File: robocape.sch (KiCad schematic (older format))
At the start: 14 parts

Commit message: Schematics: PWM
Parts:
- added R? (x2): 4.7k, symbol R_Small
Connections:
- net I2C2_SCL: now also R?.2
- net I2C2_SDA: now also R?.2
- net EHRPWM2B: now reaches U?.B13 (EHRPWM2B)
- net EHRPWM2A: now reaches U?.B19 (EHRPWM2A)
- net EHRPWM0B: now reaches U?.C21 (UART2_TXD)
- net PWMGEN_OE: now reaches U?.C25 (GPIO3_21)
- net EHRPWM1A: now reaches U?.C14 (EHRPWM1A)
- net EHRPWM1B: now reaches U?.C16 (EHRPWM1B)
- net EHRPWM0A: now reaches U?.C22 (UART2_RXD)
- new net +3.3V_A: R?.1, R?.1
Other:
- note added: "0 ohm resistors \nto select address\non i2c bus: 0x54 to 0x57\n"
- note added: "I2C adresses:\nEEPROM: 0x54 to 0x57\nBarometer: 0x77\n"
- note added: "I2C pull-ups\n"
- note removed: "0 ohm resistors \nto select address\non i2c bus"
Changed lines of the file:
@@
 F5 "XBEE_RTS" I R 3925 6250 39
 F6 "XBEE_DTR" I R 3925 6300 39
+F7 "I2C2_SDA" I R 3925 6400 39
+F8 "I2C2_SCL" I R 3925 6450 39
+F9 "PWMGEN_OE" I R 3925 6500 39
+F10 "PWM_0" I R 3925 6600 39
+F11 "PWM_1" I R 3925 6650 39
+F12 "PWM_3" I R 3925 6750 39
+F13 "PWM_4" I R 3925 6800 39
+F14 "PWM_2" I R 3925 6700 39
+F15 "PWM_5" I R 3925 6850 39
 $EndSheet
 $Sheet
@@
 	9775 1200 9775 1225
 Text Notes 10250 1400 0    39   ~ 0
-0 ohm resistors \nto select address\non i2c bus
+0 ohm resistors \nto select address\non i2c bus: 0x54 to 0x57\n
 Wire Wire Line
 	9475 1925 9425 1925
@@
 Wire Wire Line
 	4700 2875 4750 2875
+Text Notes 1200 4700 0    47   ~ 0
+I2C adresses:\nEEPROM:	0x54 to 0x57\nBarometer:	0x77\n
+Text Label 8475 3550 2    39   ~ 0
+I2C2_SDA
+Text Label 8475 3600 2    39   ~ 0
+I2C2_SCL
+$Comp
+L R_Small R?
+U 1 1 55A80D7C
+P 8575 3400
+F 0 "R?" H 8605 3420 50  0000 L CNN
+F 1 "4.7k" H 8605 3360 50  0000 L CNN
+F 2 "" H 8575 3400 60  0000 C CNN
+F 3 "" H 8575 3400 60  0000 C CNN
+	1    8575 3400
+	1    0    0    -1
+$EndComp
+$Comp
+L R_Small R?
+U 1 1 55A80E92
+P 8825 3400
+F 0 "R?" H 8855 3420 50  0000 L CNN
+F 1 "4.7k" H 8855 3360 50  0000 L CNN
+F 2 "" H 8825 3400 60  0000 C CNN
+F 3 "" H 8825 3400 60  0000 C CNN
+	1    8825 3400
+	1    0    0    -1
+$EndComp
+Wire Wire Line
+	8475 3550 8575 3550
+Wire Wire Line
+	8575 3550 8575 3500
+Wire Wire Line
+	8475 3600 8825 3600
+Wire Wire Line
+	8825 3600 8825 3500
+$Comp
+L +3.3V_A #PWR?
+U 1 1 55A80FFB
+P 8575 3250
+F 0 "#PWR?" H 8575 3210 30  0001 C CNN
+F 1 "+3.3V_A" H 8575 3360 30  0000 C CNN
+F 2 "" H 8575 3250 60  0000 C CNN
+F 3 "" H 8575 3250 60  0000 C CNN
+	1    8575 3250
+	1    0    0    -1
+$EndComp
+Wire Wire Line
+	8575 3250 8575 3300
+$Comp
+L +3.3V_A #PWR?
+U 1 1 55A810F5
+P 8825 3250
+F 0 "#PWR?" H 8825 3210 30  0001 C CNN
+F 1 "+3.3V_A" H 8825 3360 30  0000 C CNN
+F 2 "" H 8825 3250 60  0000 C CNN
+F 3 "" H 8825 3250 60  0000 C CNN
+	1    8825 3250
+	1    0    0    -1
+$EndComp
+Wire Wire Line
+	8825 3250 8825 3300
+Text Notes 8200 3050 0    39   ~ 0
+I2C pull-ups\n
+Text Label 6550 2575 0    39   ~ 0
+EHRPWM0A
+Wire Wire Line
+	6550 2575 6500 2575
+Text Label 4700 2575 2    39   ~ 0
+EHRPWM0B
+Wire Wire Line
+	4700 2575 4750 2575
+Text Label 6550 2175 0    39   ~ 0
+EHRPWM1A
+Text Label 6550 2275 0    39   ~ 0
+EHRPWM1B
+Wire Wire Line
+	6550 2275 6500 2275
+Wire Wire Line
+	6500 2175 6550 2175
+Text Label 1750 2475 2    39   ~ 0
+EHRPWM2A
+Wire Wire Line
+	1800 2475 1750 2475
+Text Label 1750 2175 2    39   ~ 0
+EHRPWM2B
+Wire Wire Line
+	1750 2175 1800 2175
+Text Label 3975 6600 0    39   ~ 0
+EHRPWM0A
+Wire Wire Line
+	3975 6600 3925 6600
+Text Label 3975 6650 0    39   ~ 0
+EHRPWM0B
+Text Label 3975 6700 0    39   ~ 0
+EHRPWM1A
+Text Label 3975 6750 0    39   ~ 0
+EHRPWM1B
+Text Label 3975 6800 0    39   ~ 0
+EHRPWM2A
+Text Label 3975 6850 0    39   ~ 0
+EHRPWM2B
+Wire Wire Line
+	3975 6650 3925 6650
+Wire Wire Line
+	3925 6700 3975 6700
+Wire Wire Line
+	3975 6750 3925 6750
+Wire Wire Line
+	3925 6800 3975 6800
+Wire Wire Line
+	3975 6850 3925 6850
+Text Label 3975 6400 0    39   ~ 0
+I2C2_SDA
+Wire Wire Line
+	3975 6400 3925 6400
+Text Label 3975 6450 0    39   ~ 0
+I2C2_SCL
+Wire Wire Line
+	3975 6450 3925 6450
+Text Label 3975 6500 0    39   ~ 0
+PWMGEN_OE
+Wire Wire Line
+	3975 6500 3925 6500
+Text Label 4700 2775 2    39   ~ 0
+PWMGEN_OE
+Wire Wire Line
+	4700 2775 4750 2775
 $EndSCHEMATC

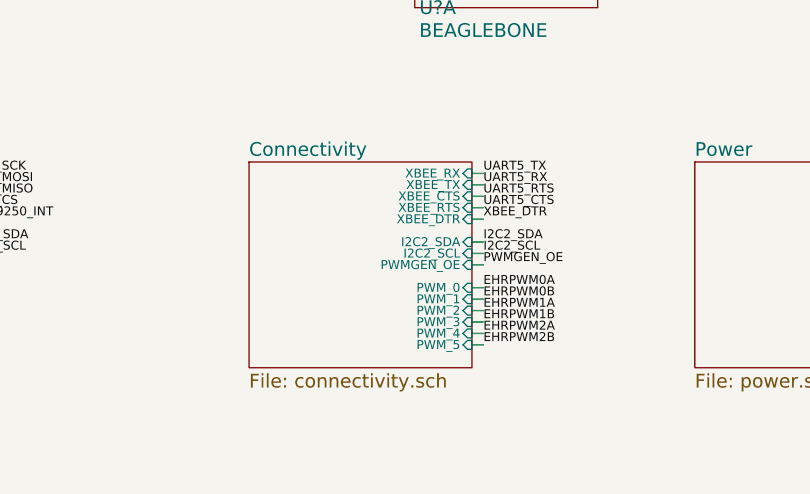
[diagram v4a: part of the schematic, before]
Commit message: Schematics: CAN
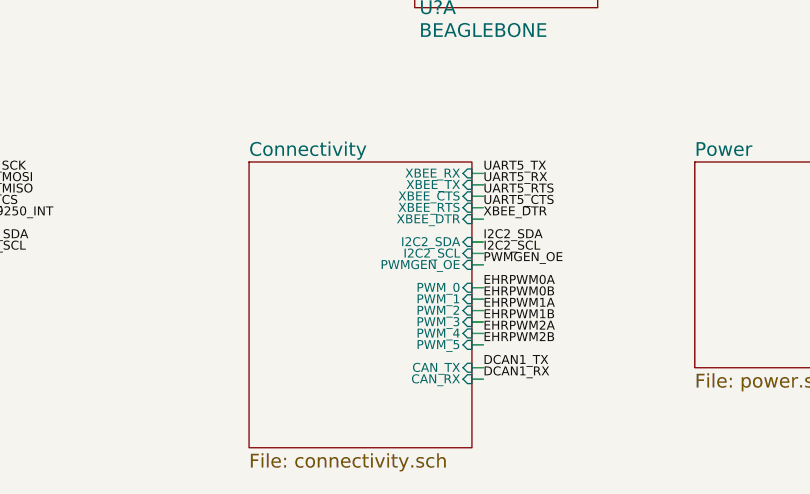
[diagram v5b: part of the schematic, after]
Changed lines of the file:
@@
 $EndComp
 $Sheet
-S 2950 6050 975  900
+S 2950 6050 975  1250
 U 55A505CD
 F0 "Connectivity" 60
@@
 F14 "PWM_2" I R 3925 6700 39
 F15 "PWM_5" I R 3925 6850 39
+F16 "CAN_TX" I R 3925 6950 39
+F17 "CAN_RX" I R 3925 7000 39
 $EndSheet
 $Sheet
@@
 Wire Wire Line
 	4700 2775 4750 2775
+Text Label 3975 7000 0    39   ~ 0
+DCAN1_RX
+Text Label 3975 6950 0    39   ~ 0
+DCAN1_TX
+Wire Wire Line
+	3975 6950 3925 6950
+Wire Wire Line
+	3925 7000 3975 7000
 $EndSCHEMATC

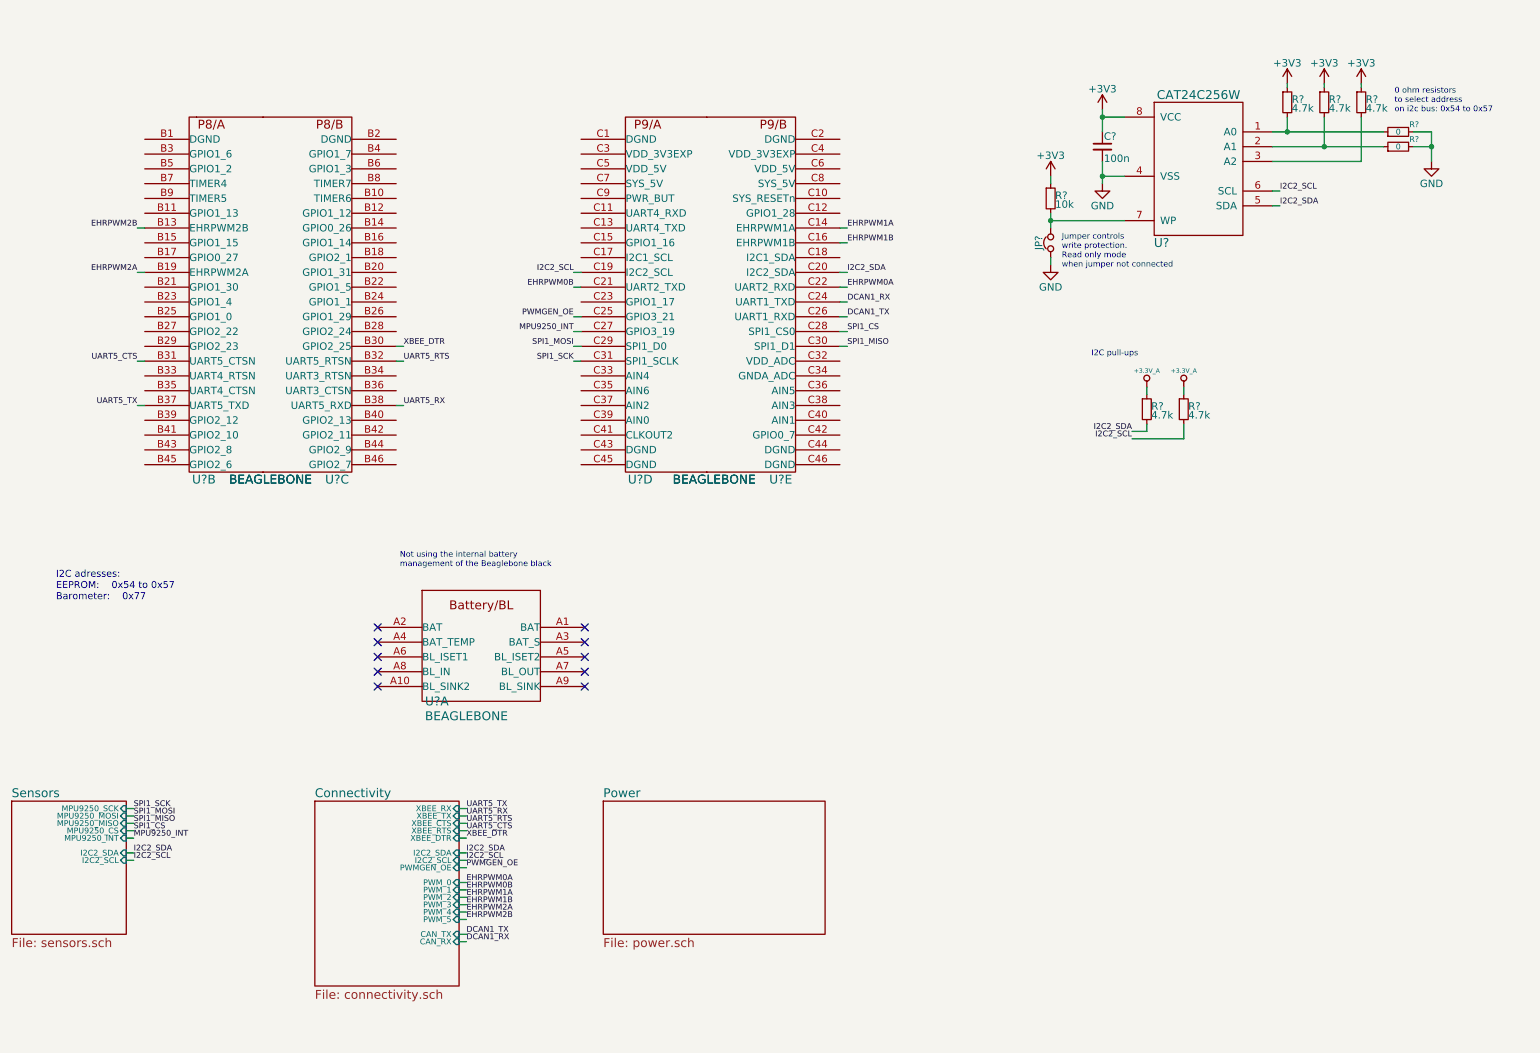
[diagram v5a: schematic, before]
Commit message: Schematics: GPS, Backup battery & Load Switch
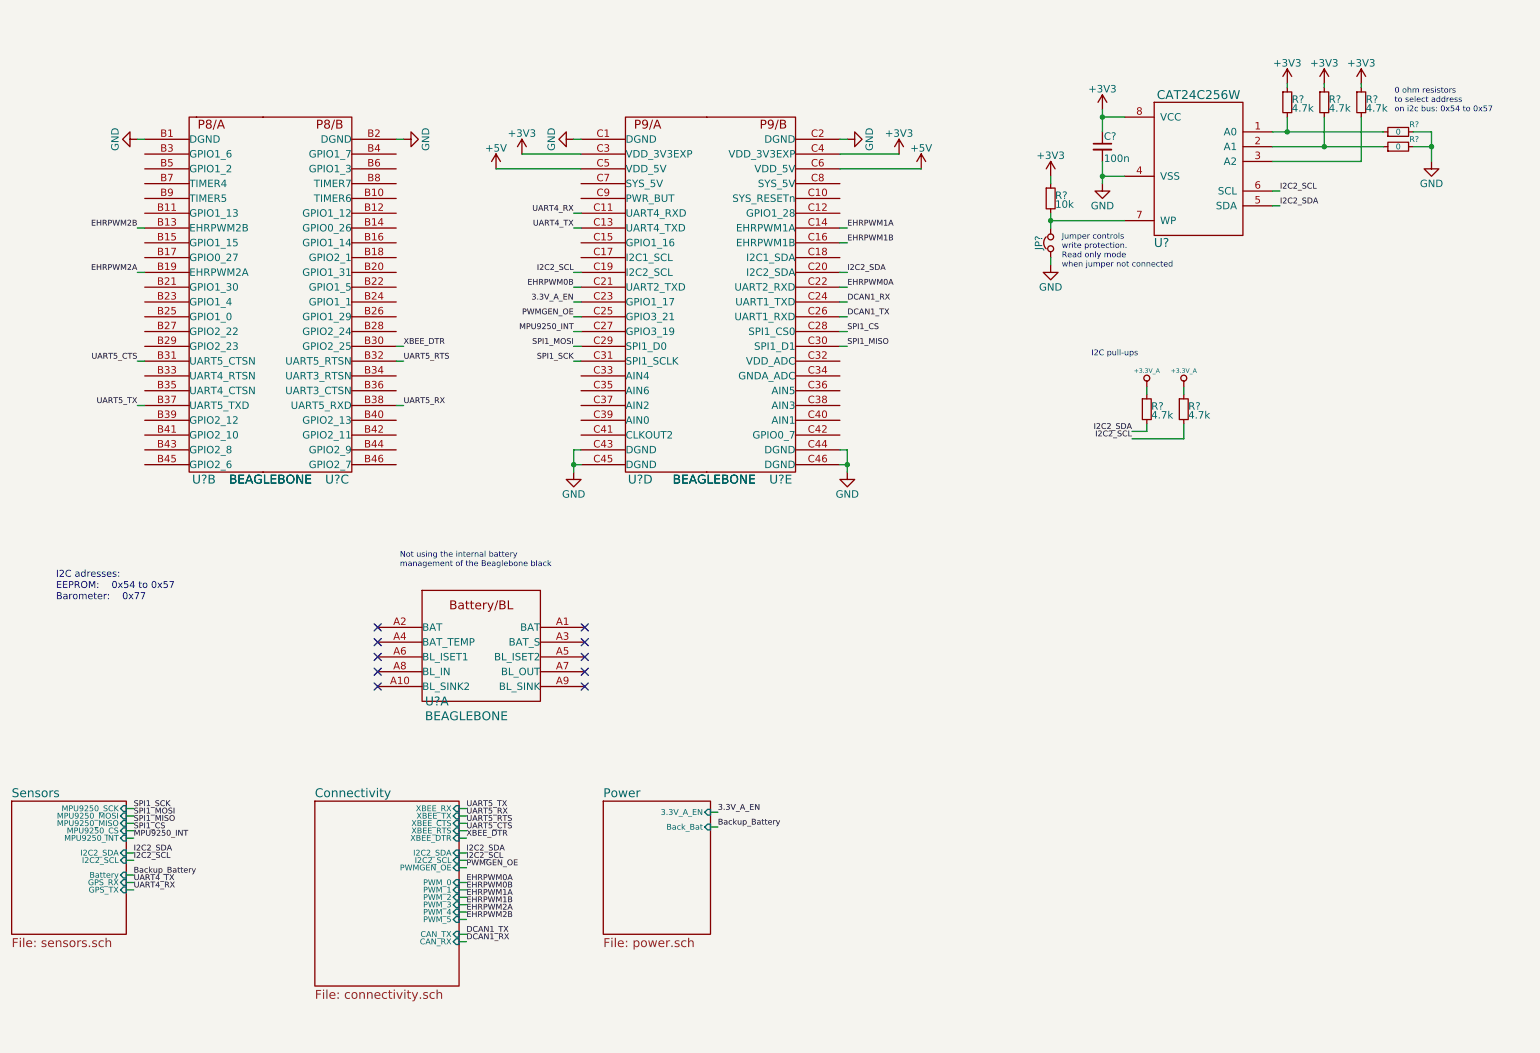
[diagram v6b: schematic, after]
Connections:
- net +3V3: now also U?.C3 (VDD_3V3EXP), U?.C4 (VDD_3V3EXP)
- net GND: now also U?.B1 (DGND), U?.B2 (DGND), U?.C1 (DGND), U?.C2 (DGND), U?.C43 (DGND), U?.C44 (DGND), U?.C45 (DGND), U?.C46 (DGND)
- net UART4_RX: now reaches U?.C11 (UART4_RXD)
- net UART4_TX: now reaches U?.C13 (UART4_TXD)
- net 3.3V_A_EN: now reaches U?.C23 (GPIO1_17)
- net +5V: now reaches U?.C5 (VDD_5V)
- net +5V: now also U?.C6 (VDD_5V)
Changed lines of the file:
@@
 $EndSheet
 $Sheet
-S 4900 6050 1500 900
+S 4900 6050 725  900
 U 55A505D5
 F0 "Power" 60
 F1 "power.sch" 60
+F2 "3.3V_A_EN" I R 5625 6125 39
+F3 "Back_Bat" I R 5625 6225 39
 $EndSheet
 $Comp
@@
 F7 "MPU9250_MISO" I R 1675 6200 39
 F8 "MPU9250_CS" I R 1675 6250 39
+F9 "GPS_TX" I R 1675 6650 39
+F10 "GPS_RX" I R 1675 6600 39
+F11 "Battery" I R 1675 6550 39
 $EndSheet
 Text Label 1725 6400 0    39   ~ 0
@@
 Wire Wire Line
 	3925 7000 3975 7000
+$Comp
+L +5V #PWR?
+U 1 1 55ABC5F4
+P 4175 1775
+F 0 "#PWR?" H 4175 1625 50  0001 C CNN
+F 1 "+5V" H 4175 1915 50  0000 C CNN
+F 2 "" H 4175 1775 60  0000 C CNN
+F 3 "" H 4175 1775 60  0000 C CNN
+	1    4175 1775
+	-1   0    0    -1
+$EndComp
+Wire Wire Line
+	7050 1775 6500 1775
+$Comp
+L +5V #PWR?
+U 1 1 55ABC86A
+P 7050 1775
+F 0 "#PWR?" H 7050 1625 50  0001 C CNN
+F 1 "+5V" H 7050 1915 50  0000 C CNN
+F 2 "" H 7050 1775 60  0000 C CNN
+F 3 "" H 7050 1775 60  0000 C CNN
+	1    7050 1775
+	-1   0    0    -1
+$EndComp
+Wire Wire Line
+	4175 1775 4750 1775
+$Comp
+L GND #PWR?
+U 1 1 55ABD079
+P 6550 1575
+F 0 "#PWR?" H 6550 1325 50  0001 C CNN
+F 1 "GND" H 6550 1425 50  0000 C CNN
+F 2 "" H 6550 1575 60  0000 C CNN
+F 3 "" H 6550 1575 60  0000 C CNN
+	1    6550 1575
+	0    -1   -1   0
+$EndComp
+Wire Wire Line
+	6550 1575 6500 1575
+$Comp
+L GND #PWR?
+U 1 1 55ABD1F2
+P 4700 1575
+F 0 "#PWR?" H 4700 1325 50  0001 C CNN
+F 1 "GND" H 4700 1425 50  0000 C CNN
+F 2 "" H 4700 1575 60  0000 C CNN
+F 3 "" H 4700 1575 60  0000 C CNN
+	1    4700 1575
+	0    1    1    0
+$EndComp
+Wire Wire Line
+	4700 1575 4750 1575
+$Comp
+L GND #PWR?
+U 1 1 55ABD7FF
+P 4700 3825
+F 0 "#PWR?" H 4700 3575 50  0001 C CNN
+F 1 "GND" H 4700 3675 50  0000 C CNN
+F 2 "" H 4700 3825 60  0000 C CNN
+F 3 "" H 4700 3825 60  0000 C CNN
+	1    4700 3825
+	1    0    0    -1
+$EndComp
+Wire Wire Line
+	4700 3675 4700 3825
+Wire Wire Line
+	4700 3775 4750 3775
+Wire Wire Line
+	4700 3675 4750 3675
+Connection ~ 4700 3775
+$Comp
+L GND #PWR?
+U 1 1 55ABDB6D
+P 6550 3825
+F 0 "#PWR?" H 6550 3575 50  0001 C CNN
+F 1 "GND" H 6550 3675 50  0000 C CNN
+F 2 "" H 6550 3825 60  0000 C CNN
+F 3 "" H 6550 3825 60  0000 C CNN
+	1    6550 3825
+	1    0    0    -1
+$EndComp
+Wire Wire Line
+	6550 3675 6550 3825
+Wire Wire Line
+	6550 3775 6500 3775
+Wire Wire Line
+	6500 3675 6550 3675
+Connection ~ 6550 3775
+$Comp
+L GND #PWR?
+U 1 1 55ABE52B
+P 3550 1575
+F 0 "#PWR?" H 3550 1325 50  0001 C CNN
+F 1 "GND" H 3550 1425 50  0000 C CNN
+F 2 "" H 3550 1575 60  0000 C CNN
+F 3 "" H 3550 1575 60  0000 C CNN
+	1    3550 1575
+	0    -1   -1   0
+$EndComp
+Wire Wire Line
+	3550 1575 3500 1575
+$Comp
+L GND #PWR?
+U 1 1 55ABE7A9
+P 1750 1575
+F 0 "#PWR?" H 1750 1325 50  0001 C CNN
+F 1 "GND" H 1750 1425 50  0000 C CNN
+F 2 "" H 1750 1575 60  0000 C CNN
+F 3 "" H 1750 1575 60  0000 C CNN
+	1    1750 1575
+	0    1    1    0
+$EndComp
+Wire Wire Line
+	1800 1575 1750 1575
+$Comp
+L +3V3 #PWR?
+U 1 1 55ABF0F8
+P 6900 1675
+F 0 "#PWR?" H 6900 1525 50  0001 C CNN
+F 1 "+3V3" H 6900 1815 50  0000 C CNN
+F 2 "" H 6900 1675 60  0000 C CNN
+F 3 "" H 6900 1675 60  0000 C CNN
+	1    6900 1675
+	1    0    0    -1
+$EndComp
+Wire Wire Line
+	6900 1675 6500 1675
+$Comp
+L +3V3 #PWR?
+U 1 1 55ABF4FC
+P 4350 1675
+F 0 "#PWR?" H 4350 1525 50  0001 C CNN
+F 1 "+3V3" H 4350 1815 50  0000 C CNN
+F 2 "" H 4350 1675 60  0000 C CNN
+F 3 "" H 4350 1675 60  0000 C CNN
+	1    4350 1675
+	1    0    0    -1
+$EndComp
+Wire Wire Line
+	4350 1675 4750 1675
+Text Label 5675 6125 0    39   ~ 0
+3.3V_A_EN
+Wire Wire Line
+	5675 6125 5625 6125
+Text Label 4700 2675 2    39   ~ 0
+3.3V_A_EN
+Wire Wire Line
+	4700 2675 4750 2675
+Text Label 4700 2075 2    39   ~ 0
+UART4_RX
+Wire Wire Line
+	4700 2075 4750 2075
+Text Label 4700 2175 2    39   ~ 0
+UART4_TX
+Wire Wire Line
+	4700 2175 4750 2175
+Text Label 1725 6600 0    39   ~ 0
+UART4_TX
+Wire Wire Line
+	1725 6600 1675 6600
+Text Label 1725 6650 0    39   ~ 0
+UART4_RX
+Wire Wire Line
+	1675 6650 1725 6650
+Text Label 1725 6550 0    39   ~ 0
+Backup_Battery
+Wire Wire Line
+	1725 6550 1675 6550
+Text Label 5675 6225 0    39   ~ 0
+Backup_Battery
+Wire Wire Line
+	5675 6225 5625 6225
 $EndSCHEMATC
